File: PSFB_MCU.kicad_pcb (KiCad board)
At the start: 4 copper layers, 83 parts, among them Q1 WMM043N10HGD, Q2 WMM043N10HGD, Q3 WMM043N10HGD, Q4 WMM043N10HGD, U3 AMS1117-3.3, U4 LM5176PWP, U5 AMS1117-5.0

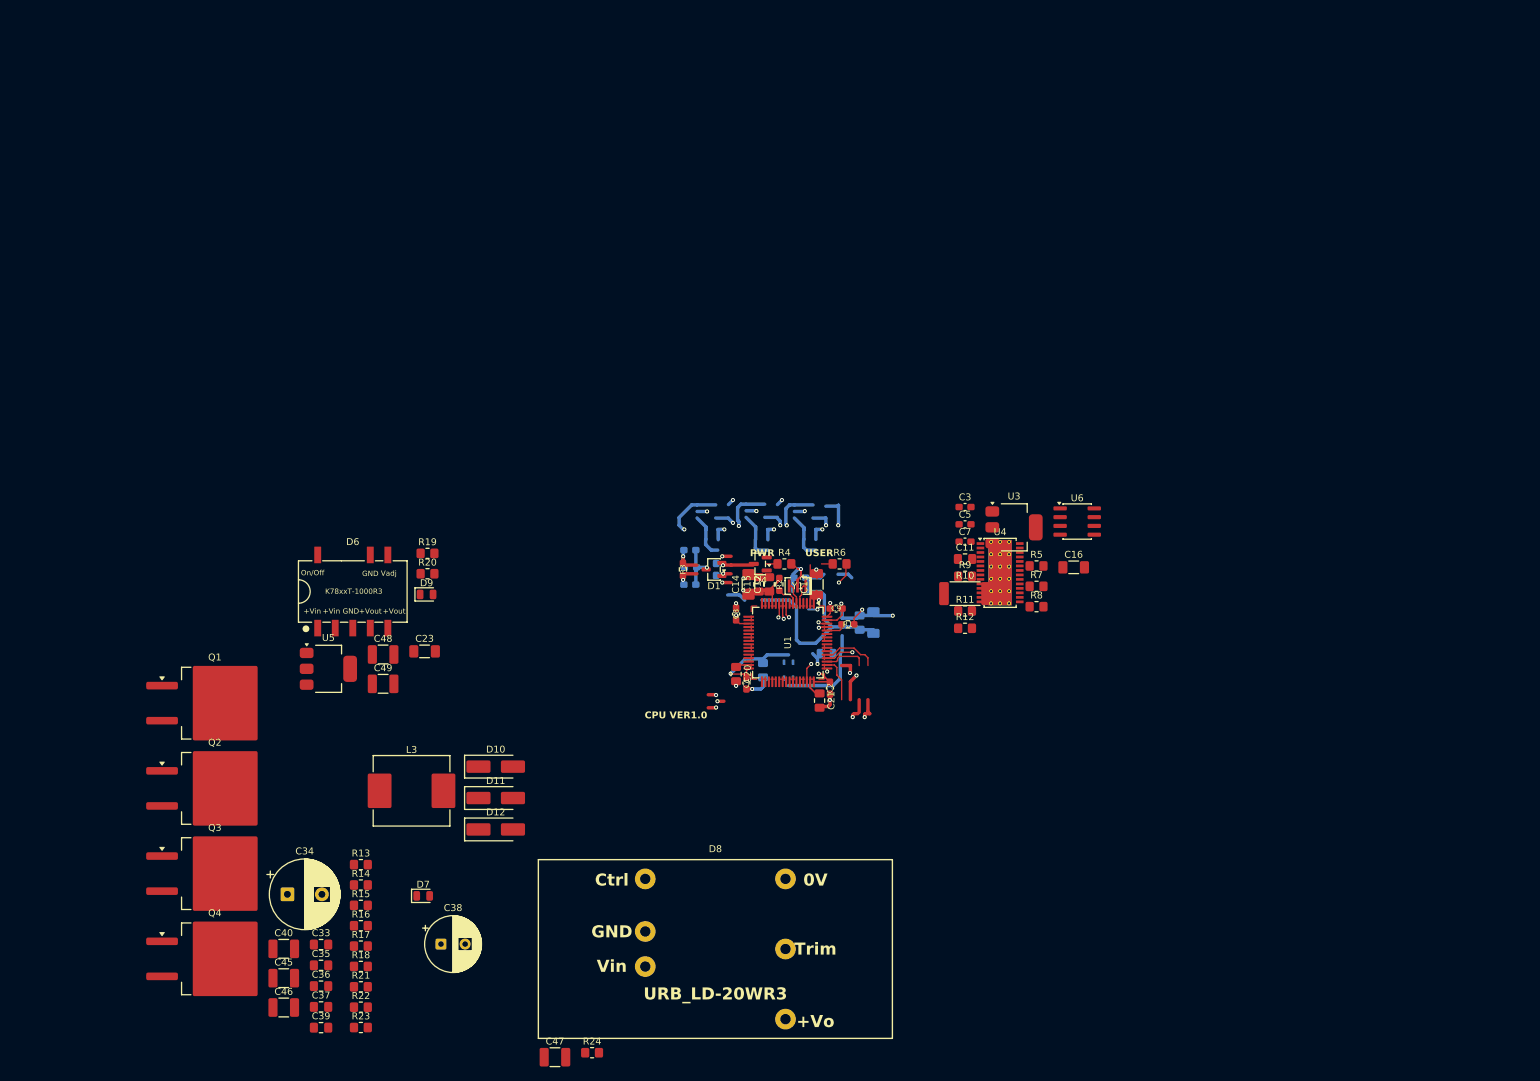
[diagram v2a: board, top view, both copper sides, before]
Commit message: VER1.0: добавил 4 канала управления драйверами
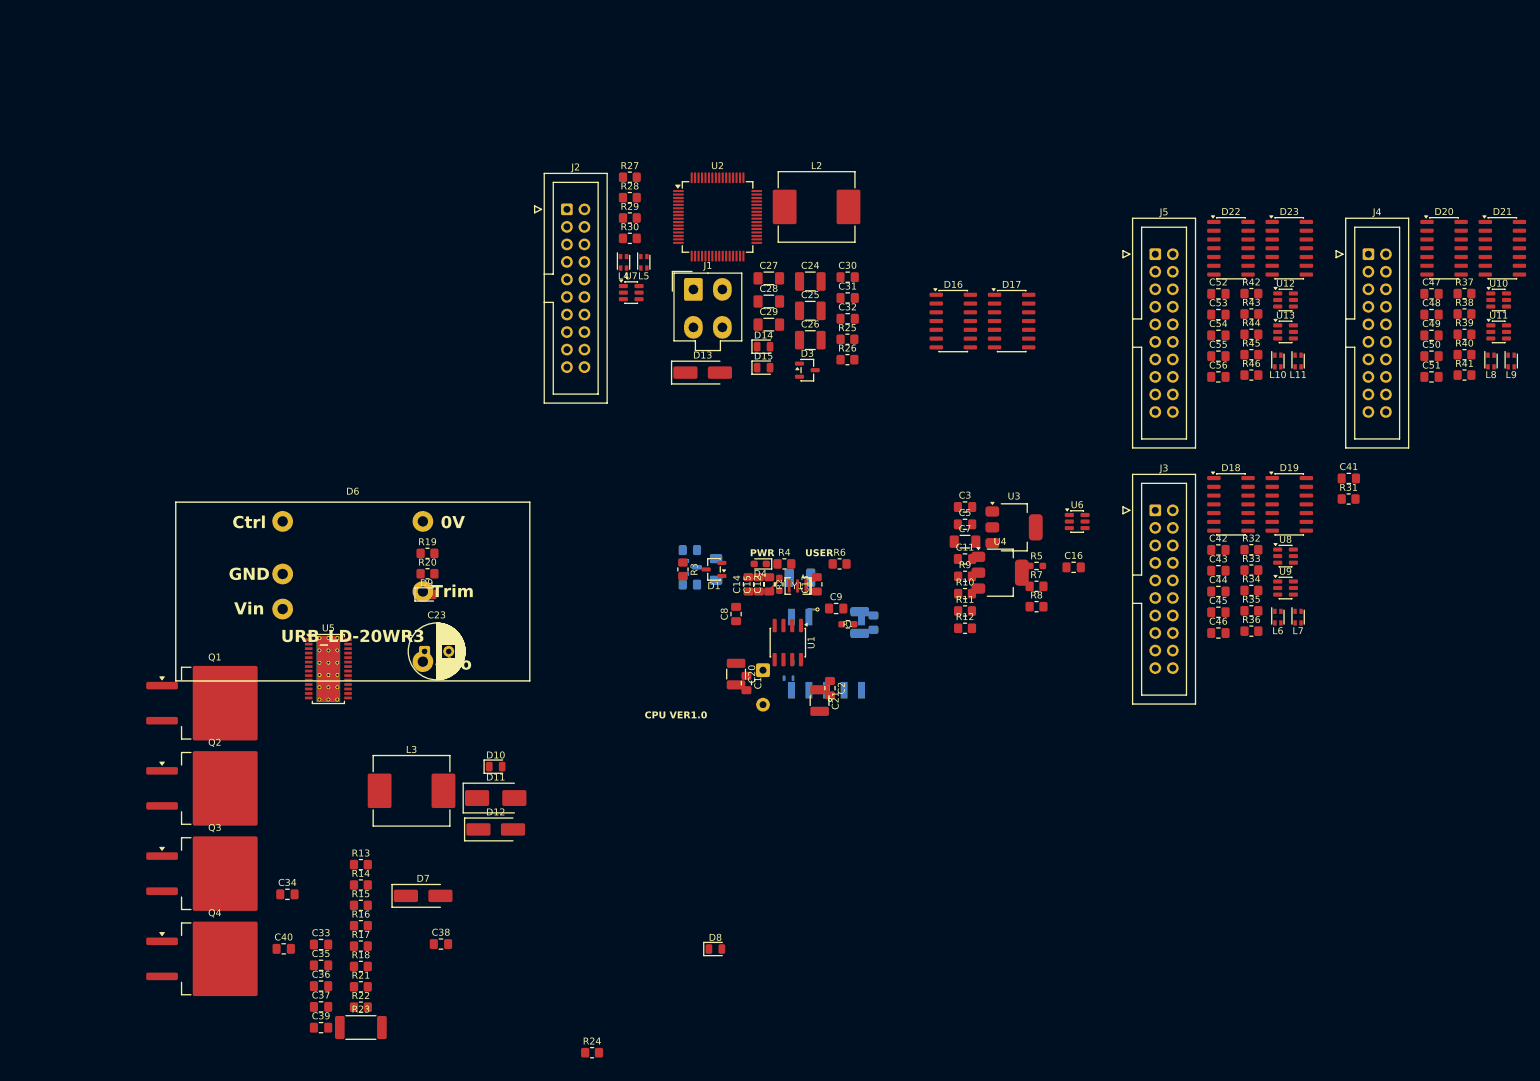
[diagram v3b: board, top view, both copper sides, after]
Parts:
- added C24: 10u, Capacitor_SMD:C_1210_3225Metric_Pad1.33x2.70mm_HandSolder, F.Cu at (151.3, 51.6)
- added C25: 10u, Capacitor_SMD:C_1210_3225Metric_Pad1.33x2.70mm_HandSolder, F.Cu at (151.3, 55.8)
- added C26: 10u, Capacitor_SMD:C_1210_3225Metric_Pad1.33x2.70mm_HandSolder, F.Cu at (151.3, 60.1)
- added C27: 10u, Capacitor_SMD:C_1206_3216Metric_Pad1.33x1.80mm_HandSolder, F.Cu at (145.2, 51.1)
- added C28: 10u, Capacitor_SMD:C_1206_3216Metric_Pad1.33x1.80mm_HandSolder, F.Cu at (145.2, 54.5)
- added C29: 10u, Capacitor_SMD:C_1206_3216Metric_Pad1.33x1.80mm_HandSolder, F.Cu at (145.2, 57.8)
- added C30: 33n, Capacitor_SMD:C_0805_2012Metric_Pad1.18x1.45mm_HandSolder, F.Cu at (156.7, 51.0)
- added C31: 100n, Capacitor_SMD:C_0805_2012Metric_Pad1.18x1.45mm_HandSolder, F.Cu at (156.7, 54.0)
- added C32: 560p, Capacitor_SMD:C_0805_2012Metric_Pad1.18x1.45mm_HandSolder, F.Cu at (156.7, 57.0)
- added C41: 10n, Capacitor_SMD:C_0805_2012Metric_Pad1.18x1.45mm_HandSolder, F.Cu at (229.3, 80.1)
- added C42: 100n, Capacitor_SMD:C_0805_2012Metric_Pad1.18x1.45mm_HandSolder, F.Cu at (210.4, 90.5)
- added C43: 4.7u, Capacitor_SMD:C_0805_2012Metric_Pad1.18x1.45mm_HandSolder, F.Cu at (210.4, 93.5)
- added C44: 100n, Capacitor_SMD:C_0805_2012Metric_Pad1.18x1.45mm_HandSolder, F.Cu at (210.4, 96.5)
- added C50: 4.7u, Capacitor_SMD:C_0805_2012Metric_Pad1.18x1.45mm_HandSolder, F.Cu at (241.3, 62.4)
- added C51: 10n, Capacitor_SMD:C_0805_2012Metric_Pad1.18x1.45mm_HandSolder, F.Cu at (241.3, 65.4)
- added C52: 100n, Capacitor_SMD:C_0805_2012Metric_Pad1.18x1.45mm_HandSolder, F.Cu at (210.4, 53.4)
- added C53: 4.7u, Capacitor_SMD:C_0805_2012Metric_Pad1.18x1.45mm_HandSolder, F.Cu at (210.4, 56.4)
- added C54: 100n, Capacitor_SMD:C_0805_2012Metric_Pad1.18x1.45mm_HandSolder, F.Cu at (210.4, 59.4)
- added C55: 4.7u, Capacitor_SMD:C_0805_2012Metric_Pad1.18x1.45mm_HandSolder, F.Cu at (210.4, 62.4)
- added C56: 10n, Capacitor_SMD:C_0805_2012Metric_Pad1.18x1.45mm_HandSolder, F.Cu at (210.4, 65.4)
- added D13: D_Schottky_Small, Diode_SMD:D_SMA_Handsoldering, F.Cu at (135.7, 64.8)
- added D14: ~, LED_SMD:LED_0805_2012Metric, F.Cu at (144.5, 61.0)
- added D15: ~, LED_SMD:LED_0805_2012Metric, F.Cu at (144.5, 64.1)
- added D16: DS90LV019, Package_SO:SO-14_3.9x8.65mm_P1.27mm, F.Cu at (172.0, 57.3)
- added D17: DS90LV019, Package_SO:SO-14_3.9x8.65mm_P1.27mm, F.Cu at (180.4, 57.3)
- added D18: DS90LV019, Package_SO:SO-14_3.9x8.65mm_P1.27mm, F.Cu at (212.2, 83.9)
- added D19: DS90LV019, Package_SO:SO-14_3.9x8.65mm_P1.27mm, F.Cu at (220.7, 83.9)
- added D20: DS90LV019, Package_SO:SO-14_3.9x8.65mm_P1.27mm, F.Cu at (243.1, 46.8)
- added D21: DS90LV019, Package_SO:SO-14_3.9x8.65mm_P1.27mm, F.Cu at (251.5, 46.8)
- added D22: DS90LV019, Package_SO:SO-14_3.9x8.65mm_P1.27mm, F.Cu at (212.2, 46.8)
- added D23: DS90LV019, Package_SO:SO-14_3.9x8.65mm_P1.27mm, F.Cu at (220.7, 46.8)
- added D3: ~, Package_TO_SOT_SMD:SOT-23-3, F.Cu at (150.8, 64.4)
- added J1: Power_IN, Connector_Molex:Molex_Mini-Fit_Jr_5566-04A_2x02_P4.20mm_Vertical, F.Cu at (134.3, 52.7)
- added J2: PSFB_Control_1, Connector_IDC:IDC-Header_2x10_P2.54mm_Vertical, F.Cu at (116.0, 41.1)
- added J3: PSFB_Control_1, Connector_IDC:IDC-Header_2x10_P2.54mm_Vertical, F.Cu at (201.2, 84.7)
- added J4: PSFB_Control_1, Connector_IDC:IDC-Header_2x10_P2.54mm_Vertical, F.Cu at (232.1, 47.6)
- added J5: PSFB_Control_1, Connector_IDC:IDC-Header_2x10_P2.54mm_Vertical, F.Cu at (201.2, 47.6)
- added L10: DLW21SN900SQ2L, Inductor_SMD:L_CommonModeChoke_Coilcraft_0805USB, F.Cu at (219.0, 63.1)
- added L11: DLW21SN900SQ2L, Inductor_SMD:L_CommonModeChoke_Coilcraft_0805USB, F.Cu at (221.9, 63.1)
- added L2: 10u, Inductor_SMD:L_Panasonic_PCC-M1040ML, F.Cu at (152.2, 40.8)
- added L4: DLW21SN900SQ2L, Inductor_SMD:L_CommonModeChoke_Coilcraft_0805USB, F.Cu at (124.2, 48.8)
- added L5: DLW21SN900SQ2L, Inductor_SMD:L_CommonModeChoke_Coilcraft_0805USB, F.Cu at (127.1, 48.8)
- added L6: DLW21SN900SQ2L, Inductor_SMD:L_CommonModeChoke_Coilcraft_0805USB, F.Cu at (219.0, 100.2)
- added L7: DLW21SN900SQ2L, Inductor_SMD:L_CommonModeChoke_Coilcraft_0805USB, F.Cu at (221.9, 100.2)
- added L8: DLW21SN900SQ2L, Inductor_SMD:L_CommonModeChoke_Coilcraft_0805USB, F.Cu at (249.9, 63.1)
- added L9: DLW21SN900SQ2L, Inductor_SMD:L_CommonModeChoke_Coilcraft_0805USB, F.Cu at (252.8, 63.1)
- added R25: 3k, Resistor_SMD:R_0805_2012Metric_Pad1.20x1.40mm_HandSolder, F.Cu at (156.6, 60.0)
- added R26: 3k, Resistor_SMD:R_0805_2012Metric_Pad1.20x1.40mm_HandSolder, F.Cu at (156.6, 62.9)
- added R27: 0, Resistor_SMD:R_0805_2012Metric_Pad1.20x1.40mm_HandSolder, F.Cu at (125.1, 36.5)
- added R28: 0, Resistor_SMD:R_0805_2012Metric_Pad1.20x1.40mm_HandSolder, F.Cu at (125.1, 39.4)
- added R29: 470, Resistor_SMD:R_0805_2012Metric_Pad1.20x1.40mm_HandSolder, F.Cu at (125.1, 42.4)
- added R30: 0, Resistor_SMD:R_0805_2012Metric_Pad1.20x1.40mm_HandSolder, F.Cu at (125.1, 45.3)
- added R31: 0, Resistor_SMD:R_0805_2012Metric_Pad1.20x1.40mm_HandSolder, F.Cu at (229.3, 83.1)
- added R32: 0, Resistor_SMD:R_0805_2012Metric_Pad1.20x1.40mm_HandSolder, F.Cu at (215.2, 90.4)
- added R33: 0, Resistor_SMD:R_0805_2012Metric_Pad1.20x1.40mm_HandSolder, F.Cu at (215.2, 93.4)
- added R34: 470, Resistor_SMD:R_0805_2012Metric_Pad1.20x1.40mm_HandSolder, F.Cu at (215.2, 96.3)
- added R35: 0, Resistor_SMD:R_0805_2012Metric_Pad1.20x1.40mm_HandSolder, F.Cu at (215.2, 99.3)
- added R36: 0, Resistor_SMD:R_0805_2012Metric_Pad1.20x1.40mm_HandSolder, F.Cu at (215.2, 102.2)
- added R37: 0, Resistor_SMD:R_0805_2012Metric_Pad1.20x1.40mm_HandSolder, F.Cu at (246.0, 53.3)
- added R38: 0, Resistor_SMD:R_0805_2012Metric_Pad1.20x1.40mm_HandSolder, F.Cu at (246.0, 56.3)
- added R39: 470, Resistor_SMD:R_0805_2012Metric_Pad1.20x1.40mm_HandSolder, F.Cu at (246.0, 59.2)
- added R40: 0, Resistor_SMD:R_0805_2012Metric_Pad1.20x1.40mm_HandSolder, F.Cu at (246.0, 62.2)
- added R41: 0, Resistor_SMD:R_0805_2012Metric_Pad1.20x1.40mm_HandSolder, F.Cu at (246.0, 65.1)
- added R42: 0, Resistor_SMD:R_0805_2012Metric_Pad1.20x1.40mm_HandSolder, F.Cu at (215.2, 53.3)
- added R43: 0, Resistor_SMD:R_0805_2012Metric_Pad1.20x1.40mm_HandSolder, F.Cu at (215.2, 56.3)
- added R44: 470, Resistor_SMD:R_0805_2012Metric_Pad1.20x1.40mm_HandSolder, F.Cu at (215.2, 59.2)
- added R45: 0, Resistor_SMD:R_0805_2012Metric_Pad1.20x1.40mm_HandSolder, F.Cu at (215.2, 62.2)
- added R46: 0, Resistor_SMD:R_0805_2012Metric_Pad1.20x1.40mm_HandSolder, F.Cu at (215.2, 65.1)
- added U10: USBLC6-2SC6, Package_TO_SOT_SMD:SOT-23-6, F.Cu at (251.0, 54.3)
- added U11: USBLC6-2SC6, Package_TO_SOT_SMD:SOT-23-6, F.Cu at (251.0, 58.9)
- added U12: USBLC6-2SC6, Package_TO_SOT_SMD:SOT-23-6, F.Cu at (220.1, 54.3)
- added U13: USBLC6-2SC6, Package_TO_SOT_SMD:SOT-23-6, F.Cu at (220.1, 58.9)
- added U2: ~, Package_QFP:LQFP-64_10x10mm_P0.5mm, F.Cu at (137.8, 42.2)
- added U7: USBLC6-2SC6, Package_TO_SOT_SMD:SOT-23-6, F.Cu at (125.3, 53.2)
- added U8: USBLC6-2SC6, Package_TO_SOT_SMD:SOT-23-6, F.Cu at (220.1, 91.4)
- added U9: USBLC6-2SC6, Package_TO_SOT_SMD:SOT-23-6, F.Cu at (220.1, 96.0)
- C1: value 100n -> 1u; footprint Capacitor_SMD:C_0603_1608Metric_Pad1.08x0.95mm_HandSolder -> Capacitor_SMD:C_0805_2012Metric_Pad1.18x1.45mm_HandSolder
- C10, C9: value 2.2u -> 100n; footprint Capacitor_SMD:C_0603_1608Metric_Pad1.08x0.95mm_HandSolder -> Capacitor_SMD:C_0805_2012Metric_Pad1.18x1.45mm_HandSolder
- C11: value 1u -> 4.7u
- C12: value 220p -> 1u
- C13: value 10u -> 2.2u; footprint Capacitor_SMD:C_1206_3216Metric_Pad1.33x1.80mm_HandSolder -> Capacitor_SMD:C_0805_2012Metric_Pad1.18x1.45mm_HandSolder
- C14: value 0.1u -> 2.2u; footprint Capacitor_SMD:C_1206_3216Metric_Pad1.33x1.80mm_HandSolder -> Capacitor_SMD:C_0805_2012Metric_Pad1.18x1.45mm_HandSolder
- C15: value 10n -> 100n
- C16: value 10u -> 1u; footprint Capacitor_SMD:C_1206_3216Metric_Pad1.33x1.80mm_HandSolder -> Capacitor_SMD:C_0805_2012Metric_Pad1.18x1.45mm_HandSolder
- C17: value 10u -> 100n; footprint Capacitor_SMD:C_1206_3216Metric_Pad1.33x1.80mm_HandSolder -> Capacitor_SMD:C_0805_2012Metric_Pad1.18x1.45mm_HandSolder
- C18: value 100n -> 2.2u; footprint Capacitor_SMD:C_0805_2012Metric_Pad1.18x1.45mm_HandSolder -> Capacitor_SMD:C_1210_3225Metric_Pad1.33x2.70mm_HandSolder
- C19: value 47p -> 100u; footprint Capacitor_SMD:C_0805_2012Metric_Pad1.18x1.45mm_HandSolder -> Capacitor_THT:CP_Radial_D10.0mm_P5.00mm
- C2, C3, C4, C5: footprint Capacitor_SMD:C_0603_1608Metric_Pad1.08x0.95mm_HandSolder -> Capacitor_SMD:C_0805_2012Metric_Pad1.18x1.45mm_HandSolder
- C20: value 1n -> 4.7u; footprint Capacitor_SMD:C_0805_2012Metric_Pad1.18x1.45mm_HandSolder -> Capacitor_SMD:C_1210_3225Metric_Pad1.33x2.70mm_HandSolder
- C21: value 33n -> 10u; footprint Capacitor_SMD:C_0805_2012Metric_Pad1.18x1.45mm_HandSolder -> Capacitor_SMD:C_1210_3225Metric_Pad1.33x2.70mm_HandSolder
- C22: value 1u -> 10u; footprint Capacitor_SMD:C_0603_1608Metric_Pad1.08x0.95mm_HandSolder -> Capacitor_SMD:C_1210_3225Metric_Pad1.33x2.70mm_HandSolder
- C23: value 10u -> 220u; footprint Capacitor_SMD:C_1206_3216Metric_Pad1.33x1.80mm_HandSolder -> Capacitor_THT:CP_Radial_D8.0mm_P3.50mm
- C33: value 560p -> 100n
- C34: value 100u -> 220p; footprint Capacitor_THT:CP_Radial_D10.0mm_P5.00mm -> Capacitor_SMD:C_0805_2012Metric_Pad1.18x1.45mm_HandSolder
- C36: value 100n -> 47p
- C38: value 220u -> 4.7u; footprint Capacitor_THT:CP_Radial_D8.0mm_P3.50mm -> Capacitor_SMD:C_0805_2012Metric_Pad1.18x1.45mm_HandSolder
- C40: footprint Capacitor_SMD:C_1210_3225Metric_Pad1.33x2.70mm_HandSolder -> Capacitor_SMD:C_0805_2012Metric_Pad1.18x1.45mm_HandSolder
- C45, C48: value 10u -> 4.7u; footprint Capacitor_SMD:C_1210_3225Metric_Pad1.33x2.70mm_HandSolder -> Capacitor_SMD:C_0805_2012Metric_Pad1.18x1.45mm_HandSolder
- C46: value 10u -> 10n; footprint Capacitor_SMD:C_1210_3225Metric_Pad1.33x2.70mm_HandSolder -> Capacitor_SMD:C_0805_2012Metric_Pad1.18x1.45mm_HandSolder
- C47, C49: value 10u -> 100n; footprint Capacitor_SMD:C_1210_3225Metric_Pad1.33x2.70mm_HandSolder -> Capacitor_SMD:C_0805_2012Metric_Pad1.18x1.45mm_HandSolder
- C6: value 100n -> 10u; footprint Capacitor_SMD:C_0603_1608Metric_Pad1.08x0.95mm_HandSolder -> Capacitor_SMD:C_1206_3216Metric_Pad1.33x1.80mm_HandSolder
- C7: value 4.7u -> 0.1u; footprint Capacitor_SMD:C_0603_1608Metric_Pad1.08x0.95mm_HandSolder -> Capacitor_SMD:C_1206_3216Metric_Pad1.33x1.80mm_HandSolder
- C8: value 1u -> 10n; footprint Capacitor_SMD:C_0603_1608Metric_Pad1.08x0.95mm_HandSolder -> Capacitor_SMD:C_0805_2012Metric_Pad1.18x1.45mm_HandSolder
- D1: value ~ -> TD301MCANFD
- D10: value D_Schottky_Small -> ~; footprint Diode_SMD:D_SMA_Handsoldering -> LED_SMD:LED_0805_2012Metric
- D11: value D_Schottky_Small -> D_TVS_Small; footprint Diode_SMD:D_SMA_Handsoldering -> Diode_SMD:D_SMB_Handsoldering
- D2: footprint LED_SMD:LED_0603_1608Metric_Pad1.05x0.95mm_HandSolder -> Package_TO_SOT_SMD:SOT-23
- D4: footprint Package_TO_SOT_SMD:SOT-23 -> LED_SMD:LED_0603_1608Metric_Pad1.05x0.95mm_HandSolder
- D5: value ~ -> K7809T; footprint LED_SMD:LED_0805_2012Metric -> MORNSUN:K78xxT-1000R3
- D6: value K7809T -> URB2415LD-20WR3; footprint MORNSUN:K78xxT-1000R3 -> MORNSUN:URB_LD-20WR3
- D7: value ~ -> D_Schottky_Small; footprint LED_SMD:LED_0805_2012Metric -> Diode_SMD:D_SMA_Handsoldering
- D8: value URB2415LD-20WR3 -> ~; footprint MORNSUN:URB_LD-20WR3 -> LED_SMD:LED_0805_2012Metric
- R10: value 10m -> 3k; footprint Resistor_SMD:R_2512_6332Metric_Pad1.40x3.35mm_HandSolder -> Resistor_SMD:R_0805_2012Metric_Pad1.20x1.40mm_HandSolder
- R11: value 143k -> 1k
- R12: value 10k -> 249k
- R14: value 249k -> 10k
- R15: value 10 -> 240k
- R16: value 2k -> 93.1k
- R17: value 10k -> 51k
- R18: value 0 -> 143k
- R19: value 1k -> 10k
- R20: value 3k -> 10k
- R21: value 10k -> 100
- R22: value 240k -> 0
- R23: value 51k -> 10m; footprint Resistor_SMD:R_0805_2012Metric_Pad1.20x1.40mm_HandSolder -> Resistor_SMD:R_2512_6332Metric_Pad1.40x3.35mm_HandSolder
- R24: value 0 -> 100
- R3: value 1k -> 59; footprint Resistor_SMD:R_0603_1608Metric_Pad0.98x0.95mm_HandSolder -> Resistor_SMD:R_0805_2012Metric_Pad1.20x1.40mm_HandSolder
- R4: value 93.1k -> 59
- R5: value 59 -> 1k; footprint Resistor_SMD:R_0805_2012Metric_Pad1.20x1.40mm_HandSolder -> Resistor_SMD:R_0603_1608Metric_Pad0.98x0.95mm_HandSolder
- R6: value 100 -> 2k
- R7: value 59 -> 10
- R9: value 100 -> 0
- U1: footprint Package_QFP:LQFP-64_10x10mm_P0.5mm -> Package_SO:SOIC-8_3.9x4.9mm_P1.27mm
- U3: value AMS1117-3.3 -> AMS1117-5.0
- U4: value LM5176PWP -> AMS1117-3.3; footprint Package_SO:HTSSOP-28-1EP_4.4x9.7mm_P0.65mm_EP3.4x9.5mm_ThermalVias -> Package_TO_SOT_SMD:SOT-223-3_TabPin2
- U5: value AMS1117-5.0 -> LM5176PWP; footprint Package_TO_SOT_SMD:SOT-223-3_TabPin2 -> Package_SO:HTSSOP-28-1EP_4.4x9.7mm_P0.65mm_EP3.4x9.5mm_ThermalVias
- U6: value ~ -> USBLC6-2SC6; footprint Package_SO:SOIC-8_3.9x4.9mm_P1.27mm -> Package_TO_SOT_SMD:SOT-23-6
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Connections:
- C10 pad 1: Net-(U1-VCAP_2) -> +3.3V
- C11 pad 1: VCC -> +3.3V
- C11 pad 2: GND_IN -> GND
- C12 pad 1: Net-(U4-SLOPE) -> +3.3V
- C12 pad 2: GND_IN -> GND
- C13 pad 1: +3.3V -> Net-(U2-VCAP_1)
- C14 pad 1: +3.3V -> Net-(U2-VCAP_2)
- C15 pad 1: Net-(C15-Pad1) -> Net-(U5-VIN)
- C15 pad 2: GND_CAN -> GND_IN
- C16 pad 1: GND -> VCC
- C16 pad 2: +5V -> GND_IN
- C17 pad 1: GND -> +24V
- C17 pad 2: +3.3V -> GND_IN
- C18 pad 1: Net-(U4-SS) -> GND_IN
- C18 pad 2: GND_IN -> VIN_filtered
- C19 pad 1: Net-(U4-CSG) -> VIN_filtered
- C19 pad 2: Net-(U4-CS) -> GND_IN
- C20 pad 1: Net-(U4-RT/SYNC) -> GND_IN
- C20 pad 2: unconnected-(C20-Pad2) -> VIN_filtered
- C21 pad 1: Net-(U4-COMP) -> GND_IN
- C21 pad 2: Net-(C21-Pad2) -> +24V
- C22 pad 1: +3.3V -> GND_IN
- C22 pad 2: GND -> +24V
- C23 pad 1: GND -> +24V
- C23 pad 2: +5V -> GND_IN
- C33 pad 1: Net-(U4-COMP) -> /SW1
- C33 pad 2: GND_IN -> Net-(D12-K)
- C34 pad 1: VIN -> Net-(U5-SLOPE)
- C35 pad 1: Net-(U4-VIN) -> /SW2
- C35 pad 2: GND_IN -> Net-(D13-K)
- C36 pad 1: /SW1 -> Net-(U5-CSG)
- C36 pad 2: Net-(D10-K) -> Net-(U5-CS)
- C37 pad 1: /SW2 -> +3.3V
- C37 pad 2: Net-(D11-K) -> GND
- C38 pad 1: +24V -> +3.3V
- C38 pad 2: GND_IN -> GND
- C39 pad 1: +24V -> +3.3V
- C39 pad 2: GND_IN -> GND
- C40 pad 1: GND_IN -> +3.3V
- C40 pad 2: VIN -> GND
- C45 pad 1: GND_IN -> +3.3V
- C45 pad 2: +24V -> GND
- C46 pad 1: GND_IN -> /FAULT2
- C46 pad 2: +24V -> GND
- C47 pad 1: GND_IN -> +3.3V
- C47 pad 2: +24V -> GND
- C48 pad 1: GND -> +3.3V
- C48 pad 2: +9V -> GND
- C49 pad 1: GND -> +3.3V
- C49 pad 2: +15V -> GND
- C8 pad 1: +3.3V -> Net-(C8-Pad1)
- C8 pad 2: GND -> GND_CAN
- C9 pad 1: Net-(U1-VCAP_1) -> +3.3V
- D1 pad 1: SWCLK -> CAN1_RXD_MCU
- D1 pad 2: SWDIO -> CAN1_TXD_MCU
- D10 pad 2: VCC -> +3.3V
- D11 pad 1: Net-(D11-K) -> GND_IN
- D11 pad 2: VCC -> VIN_filtered
- D12 pad 2: VIN -> VCC
- D2 pad 1: Net-(D2-K) -> CANH
- D2 pad 2: Net-(D2-A) -> CANL
- D4 pad 1: CANH -> Net-(D4-K)
- D4 pad 2: CANL -> Net-(D4-A)
- D5 pad 1: Net-(D5-K) -> +15V
- D5 pad 2: +3.3V -> +15V
- D6 pad 1: +15V -> unconnected-(D6-Ctrl-Pad1)
- D6 pad 2: +15V -> GND_IN
- D6 pad 3: GND -> +24V
- D6 pad 4: +9V -> +15V
- D6 pad 5: +9V -> Net-(D6-Trim)
- D6 pad 6: unconnected-(D6-Vadj-Pad6) -> GND1
- D7 pad 2: +5V -> VIN_filtered
- D8 pad 1: unconnected-(D8-Ctrl-Pad1) -> Net-(D8-K)
- D8 pad 2: GND_IN -> +5V
- L1 pad 1: Net-(D3-CANH) -> Net-(D1-CANH)
- L1 pad 3: Net-(D3-CANL) -> Net-(D1-CANL)
- Q1 pad 2: VIN -> VIN_filtered
- Q2 pad 1: /LDRV1 -> /HDRV2
- Q2 pad 2: /SW1 -> +24V
- Q2 pad 3: Net-(Q2-S) -> /SW2
- Q3 pad 1: /HDRV2 -> /LDRV1
- Q3 pad 2: +24V -> /SW1
- Q3 pad 3: /SW2 -> Net-(Q3-S)
- Q4 pad 3: Net-(Q2-S) -> Net-(Q3-S)
- R10 pad 1: GND_IN -> Net-(D9-K)
- R10 pad 2: Net-(Q2-S) -> GND
- R11 pad 1: GND_IN -> Net-(D10-K)
- R11 pad 2: Net-(U4-RT/SYNC) -> GND
- R12 pad 1: GND_IN -> Net-(U5-EN/UVLO)
- R12 pad 2: Net-(C21-Pad2) -> VIN_filtered
- R13 pad 1: Net-(U4-EN/UVLO) -> Net-(U5-EN/UVLO)
- R14 pad 1: Net-(U4-EN/UVLO) -> GND_IN
- R14 pad 2: VIN -> Net-(C30-Pad2)
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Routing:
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- removed copper zone on F.Cu, net GND

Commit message: VER1.0: добавил схему с измерением напряжения и заменил LVDS трансиверы
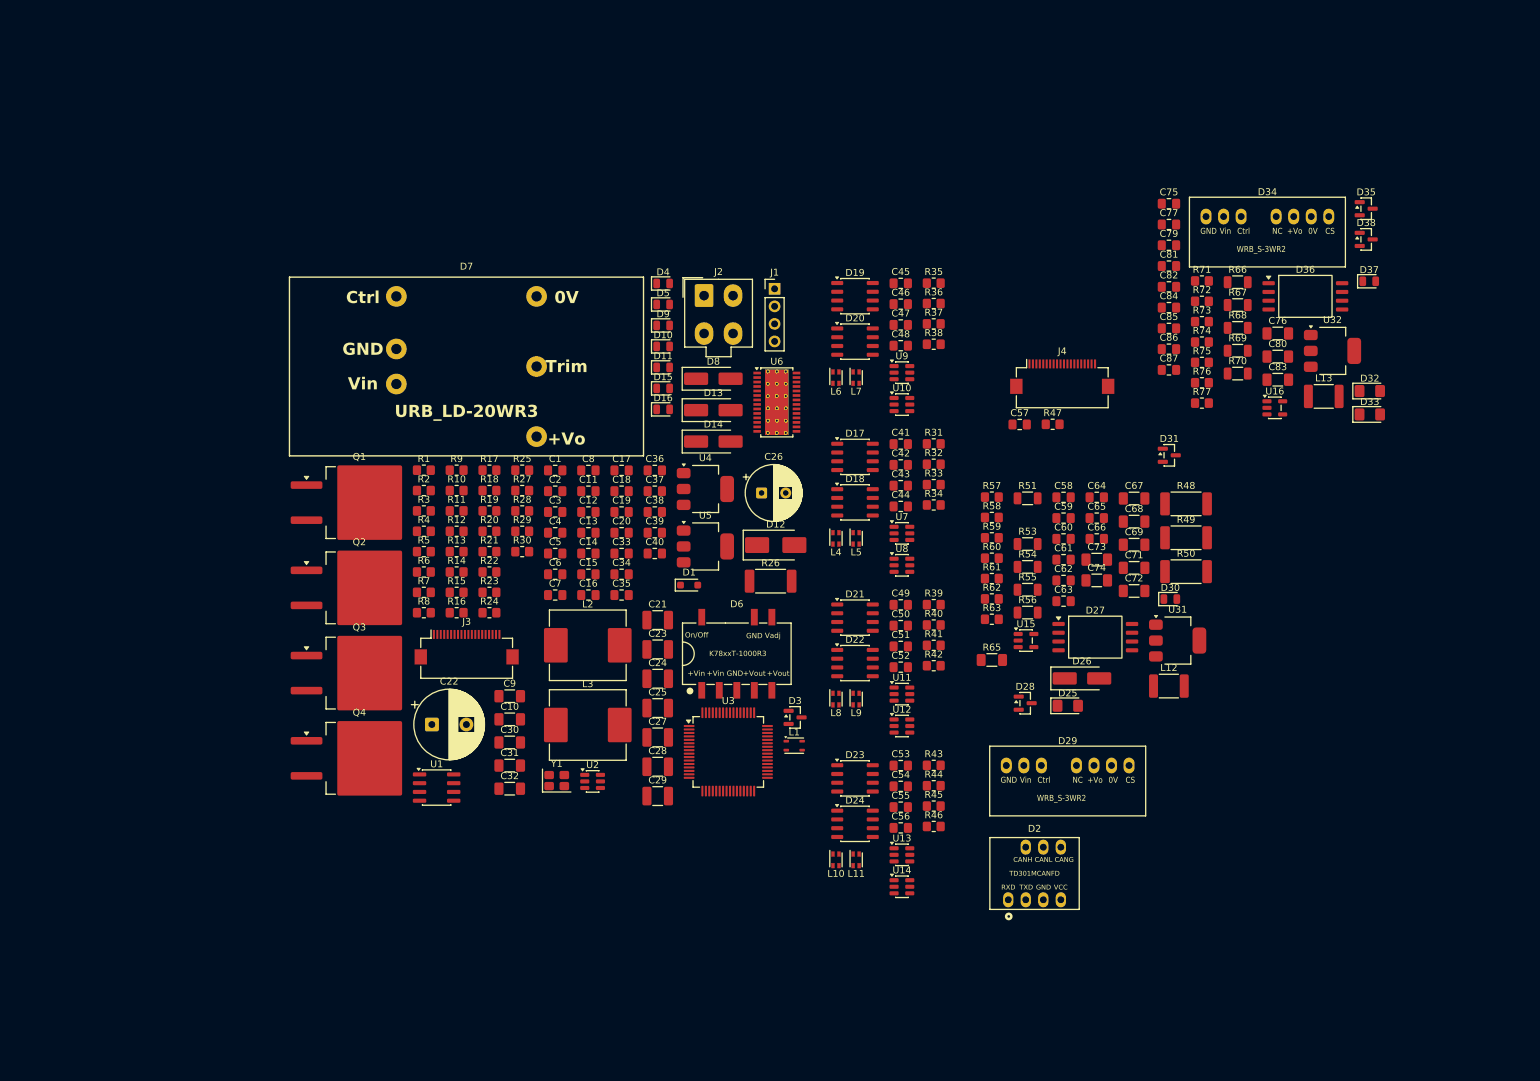
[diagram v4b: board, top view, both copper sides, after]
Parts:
- removed J5: PSFB_Control_1, Connector_IDC:IDC-Header_2x10_P2.54mm_Vertical
- added C57: 10n, Capacitor_SMD:C_0805_2012Metric_Pad1.18x1.45mm_HandSolder, F.Cu at (181.6, 72.3)
- added C58: 56p, Capacitor_SMD:C_0805_2012Metric_Pad1.18x1.45mm_HandSolder, F.Cu at (187.9, 82.8)
- added C59: 2.2u, Capacitor_SMD:C_0805_2012Metric_Pad1.18x1.45mm_HandSolder, F.Cu at (187.9, 85.9)
- added C60: 0.1u, Capacitor_SMD:C_0805_2012Metric_Pad1.18x1.45mm_HandSolder, F.Cu at (187.9, 88.9)
- added C61: 2.2u, Capacitor_SMD:C_0805_2012Metric_Pad1.18x1.45mm_HandSolder, F.Cu at (187.9, 91.9)
- added C62: 0.1u, Capacitor_SMD:C_0805_2012Metric_Pad1.18x1.45mm_HandSolder, F.Cu at (187.9, 94.9)
- added C63: 56p, Capacitor_SMD:C_0805_2012Metric_Pad1.18x1.45mm_HandSolder, F.Cu at (187.9, 97.9)
- added C64: 56p, Capacitor_SMD:C_0805_2012Metric_Pad1.18x1.45mm_HandSolder, F.Cu at (192.8, 82.8)
- added C65: 100n, Capacitor_SMD:C_0805_2012Metric_Pad1.18x1.45mm_HandSolder, F.Cu at (192.8, 85.9)
- added C66: 1n, Capacitor_SMD:C_0805_2012Metric_Pad1.18x1.45mm_HandSolder, F.Cu at (192.8, 88.9)
- added C67: 10u, Capacitor_SMD:C_1206_3216Metric_Pad1.33x1.80mm_HandSolder, F.Cu at (198.2, 83.0)
- added C68: 1u, Capacitor_SMD:C_1206_3216Metric_Pad1.33x1.80mm_HandSolder, F.Cu at (198.2, 86.4)
- added C69: 10u, Capacitor_SMD:C_1206_3216Metric_Pad1.33x1.80mm_HandSolder, F.Cu at (198.2, 89.7)
- added C71: 10u, Capacitor_SMD:C_1206_3216Metric_Pad1.33x1.80mm_HandSolder, F.Cu at (198.2, 93.1)
- added C72: 10u, Capacitor_SMD:C_1206_3216Metric_Pad1.33x1.80mm_HandSolder, F.Cu at (198.2, 96.4)
- added C73: 10u, Capacitor_SMD:C_1206_3216Metric_Pad1.33x1.80mm_HandSolder, F.Cu at (192.8, 91.9)
- added C74: 1u, Capacitor_SMD:C_1206_3216Metric_Pad1.33x1.80mm_HandSolder, F.Cu at (192.8, 94.9)
- added C75: 56p, Capacitor_SMD:C_0805_2012Metric_Pad1.18x1.45mm_HandSolder, F.Cu at (203.2, 40.3)
- added C76: 10u, Capacitor_SMD:C_1206_3216Metric_Pad1.33x1.80mm_HandSolder, F.Cu at (219.0, 59.1)
- added C77: 2.2u, Capacitor_SMD:C_0805_2012Metric_Pad1.18x1.45mm_HandSolder, F.Cu at (203.2, 43.3)
- added C79: 0.1u, Capacitor_SMD:C_0805_2012Metric_Pad1.18x1.45mm_HandSolder, F.Cu at (203.2, 46.3)
- added C80: 10u, Capacitor_SMD:C_1206_3216Metric_Pad1.33x1.80mm_HandSolder, F.Cu at (219.0, 62.5)
- added C81: 2.2u, Capacitor_SMD:C_0805_2012Metric_Pad1.18x1.45mm_HandSolder, F.Cu at (203.2, 49.3)
- added C82: 0.1u, Capacitor_SMD:C_0805_2012Metric_Pad1.18x1.45mm_HandSolder, F.Cu at (203.2, 52.4)
- added C83: 10u, Capacitor_SMD:C_1206_3216Metric_Pad1.33x1.80mm_HandSolder, F.Cu at (219.0, 65.8)
- added C84: 56p, Capacitor_SMD:C_0805_2012Metric_Pad1.18x1.45mm_HandSolder, F.Cu at (203.2, 55.4)
- added C85: 56p, Capacitor_SMD:C_0805_2012Metric_Pad1.18x1.45mm_HandSolder, F.Cu at (203.2, 58.4)
- added C86: 100n, Capacitor_SMD:C_0805_2012Metric_Pad1.18x1.45mm_HandSolder, F.Cu at (203.2, 61.4)
- added C87: 1n, Capacitor_SMD:C_0805_2012Metric_Pad1.18x1.45mm_HandSolder, F.Cu at (203.2, 64.4)
- added D24: ~, Package_SO:SO-8_3.9x4.9mm_P1.27mm, F.Cu at (157.7, 130.2)
- added D25: ~, LED_SMD:LED_1206_3216Metric_Pad1.42x1.75mm_HandSolder, F.Cu at (188.6, 113.1)
- added D26: ~, Diode_SMD:D_SMA_Handsoldering, F.Cu at (190.6, 109.1)
- added D27: ~, Package_SO:SOIC-8_7.5x5.85mm_P1.27mm, F.Cu at (192.6, 103.1)
- added D28: ~, Package_TO_SOT_SMD:SOT-23, F.Cu at (182.4, 112.7)
- added D29: ~, MORNSUN:WRB_S-3WR2, F.Cu at (188.5, 121.7)
- added D30: ~, LED_SMD:LED_0805_2012Metric, F.Cu at (203.4, 97.6)
- added D31: ~, Package_TO_SOT_SMD:SOT-23, F.Cu at (203.3, 76.8)
- added D32: ~, LED_SMD:LED_1206_3216Metric_Pad1.42x1.75mm_HandSolder, F.Cu at (232.3, 67.5)
- added D33: ~, LED_SMD:LED_1206_3216Metric_Pad1.42x1.75mm_HandSolder, F.Cu at (232.3, 70.8)
- added D34: ~, MORNSUN:WRB_S-3WR2, F.Cu at (217.5, 42.2)
- added D35: ~, Package_TO_SOT_SMD:SOT-23, F.Cu at (231.8, 41.0)
- added D36: ~, Package_SO:SOIC-8_7.5x5.85mm_P1.27mm, F.Cu at (223.0, 53.7)
- added D37: ~, LED_SMD:LED_0805_2012Metric, F.Cu at (232.2, 51.5)
- added D38: ~, Package_TO_SOT_SMD:SOT-23, F.Cu at (231.8, 45.5)
- added L12: 4.7u, Inductor_SMD:L_1812_4532Metric_Pad1.30x3.40mm_HandSolder, F.Cu at (203.2, 110.2)
- added L13: 4.7u, Inductor_SMD:L_1812_4532Metric_Pad1.30x3.40mm_HandSolder, F.Cu at (225.7, 68.2)
- added R47: 470, Resistor_SMD:R_0805_2012Metric_Pad1.20x1.40mm_HandSolder, F.Cu at (186.4, 72.3)
- added R48: 150k, Resistor_SMD:R_2512_6332Metric_Pad1.40x3.35mm_HandSolder, F.Cu at (205.7, 83.8)
- added R49: 150k, Resistor_SMD:R_2512_6332Metric_Pad1.40x3.35mm_HandSolder, F.Cu at (205.7, 88.7)
- added R50: 150k, Resistor_SMD:R_2512_6332Metric_Pad1.40x3.35mm_HandSolder, F.Cu at (205.7, 93.6)
- added R51: 2M, Resistor_SMD:R_1206_3216Metric, F.Cu at (182.7, 83.0)
- added R53: 2M, Resistor_SMD:R_1206_3216Metric, F.Cu at (182.7, 89.6)
- added R54: 2M, Resistor_SMD:R_1206_3216Metric, F.Cu at (182.7, 92.9)
- added R55: 2M, Resistor_SMD:R_1206_3216Metric, F.Cu at (182.7, 96.2)
- added R56: 11.3k, Resistor_SMD:R_1206_3216Metric, F.Cu at (182.7, 99.5)
- added R57: 120, Resistor_SMD:R_0805_2012Metric_Pad1.20x1.40mm_HandSolder, F.Cu at (177.6, 82.8)
- added R58: 1k, Resistor_SMD:R_0805_2012Metric_Pad1.20x1.40mm_HandSolder, F.Cu at (177.6, 85.8)
- added R59: 1k, Resistor_SMD:R_0805_2012Metric_Pad1.20x1.40mm_HandSolder, F.Cu at (177.6, 88.7)
- added R60: 1k, Resistor_SMD:R_0805_2012Metric_Pad1.20x1.40mm_HandSolder, F.Cu at (177.6, 91.7)
- added R61: 1k, Resistor_SMD:R_0805_2012Metric_Pad1.20x1.40mm_HandSolder, F.Cu at (177.6, 94.6)
- added R62: 510, Resistor_SMD:R_0805_2012Metric_Pad1.20x1.40mm_HandSolder, F.Cu at (177.6, 97.6)
- added R63: 750, Resistor_SMD:R_0805_2012Metric_Pad1.20x1.40mm_HandSolder, F.Cu at (177.6, 100.5)
- added R65: 10k, Resistor_SMD:R_1206_3216Metric_Pad1.30x1.75mm_HandSolder, F.Cu at (177.6, 106.4)
- added R66: 110k, Resistor_SMD:R_1206_3216Metric, F.Cu at (213.2, 51.7)
- added R67: 110k, Resistor_SMD:R_1206_3216Metric, F.Cu at (213.2, 55.0)
- added R68: 110k, Resistor_SMD:R_1206_3216Metric, F.Cu at (213.2, 58.3)
- added R69: 110k, Resistor_SMD:R_1206_3216Metric, F.Cu at (213.2, 61.6)
- added R70: 11.3k, Resistor_SMD:R_1206_3216Metric, F.Cu at (213.2, 64.9)
- added R71: 120, Resistor_SMD:R_0805_2012Metric_Pad1.20x1.40mm_HandSolder, F.Cu at (208.0, 51.5)
- added R72: 1k, Resistor_SMD:R_0805_2012Metric_Pad1.20x1.40mm_HandSolder, F.Cu at (208.0, 54.5)
- added R73: 1k, Resistor_SMD:R_0805_2012Metric_Pad1.20x1.40mm_HandSolder, F.Cu at (208.0, 57.4)
- added R74: 750, Resistor_SMD:R_0805_2012Metric_Pad1.20x1.40mm_HandSolder, F.Cu at (208.0, 60.4)
- added R75: 1k, Resistor_SMD:R_0805_2012Metric_Pad1.20x1.40mm_HandSolder, F.Cu at (208.0, 63.3)
- added R76: 1k, Resistor_SMD:R_0805_2012Metric_Pad1.20x1.40mm_HandSolder, F.Cu at (208.0, 66.2)
- added R77: 510, Resistor_SMD:R_0805_2012Metric_Pad1.20x1.40mm_HandSolder, F.Cu at (208.0, 69.2)
- added U14: USBLC6-2SC6, Package_TO_SOT_SMD:SOT-23-6, F.Cu at (164.5, 139.3)
- added U15: ~, Package_TO_SOT_SMD:SOT-23-5, F.Cu at (182.5, 103.6)
- added U16: ~, Package_TO_SOT_SMD:SOT-23-5, F.Cu at (218.6, 69.9)
- added U31: ~, Package_TO_SOT_SMD:SOT-223-3_TabPin2, F.Cu at (204.5, 103.6)
- added U32: ~, Package_TO_SOT_SMD:SOT-223-3_TabPin2, F.Cu at (226.9, 61.6)
- C10: value 100n -> 0.1u; footprint Capacitor_SMD:C_0805_2012Metric_Pad1.18x1.45mm_HandSolder -> Capacitor_SMD:C_1206_3216Metric_Pad1.33x1.80mm_HandSolder; moved to F.Cu
- C11, C40: value 4.7u -> 10n
- C12: value 1u -> 2.2u
- C14: value 2.2u -> 100n
- C16: value 1u -> 4.7u
- C17: value 100n -> 1u; moved to F.Cu
- C18: value 2.2u -> 100n; footprint Capacitor_SMD:C_1210_3225Metric_Pad1.33x2.70mm_HandSolder -> Capacitor_SMD:C_0805_2012Metric_Pad1.18x1.45mm_HandSolder; moved to F.Cu
- C19: value 100u -> 1u; footprint Capacitor_THT:CP_Radial_D10.0mm_P5.00mm -> Capacitor_SMD:C_0805_2012Metric_Pad1.18x1.45mm_HandSolder; moved to F.Cu
- C20: value 4.7u -> 100n; footprint Capacitor_SMD:C_1210_3225Metric_Pad1.33x2.70mm_HandSolder -> Capacitor_SMD:C_0805_2012Metric_Pad1.18x1.45mm_HandSolder
- C21: value 10u -> 2.2u
- C22: value 10u -> 100u; footprint Capacitor_SMD:C_1210_3225Metric_Pad1.33x2.70mm_HandSolder -> Capacitor_THT:CP_Radial_D10.0mm_P5.00mm; moved to F.Cu
- C23: value 220u -> 4.7u; footprint Capacitor_THT:CP_Radial_D8.0mm_P3.50mm -> Capacitor_SMD:C_1210_3225Metric_Pad1.33x2.70mm_HandSolder
- C26: value 10u -> 220u; footprint Capacitor_SMD:C_1210_3225Metric_Pad1.33x2.70mm_HandSolder -> Capacitor_THT:CP_Radial_D8.0mm_P3.50mm
- C27, C28, C29: footprint Capacitor_SMD:C_1206_3216Metric_Pad1.33x1.80mm_HandSolder -> Capacitor_SMD:C_1210_3225Metric_Pad1.33x2.70mm_HandSolder
- C3: value 100n -> 12p
- C30: value 33n -> 10u; footprint Capacitor_SMD:C_0805_2012Metric_Pad1.18x1.45mm_HandSolder -> Capacitor_SMD:C_1206_3216Metric_Pad1.33x1.80mm_HandSolder
- C31, C9: value 100n -> 10u; footprint Capacitor_SMD:C_0805_2012Metric_Pad1.18x1.45mm_HandSolder -> Capacitor_SMD:C_1206_3216Metric_Pad1.33x1.80mm_HandSolder
- C32: value 560p -> 10u; footprint Capacitor_SMD:C_0805_2012Metric_Pad1.18x1.45mm_HandSolder -> Capacitor_SMD:C_1206_3216Metric_Pad1.33x1.80mm_HandSolder
- C33: value 100n -> 33n
- C34: value 220p -> 100n
- C35: value 100n -> 560p
- C36: value 47p -> 100n
- C37: value 100n -> 220p
- C38, C43, C45, C50, C53: value 4.7u -> 100n
- C39: value 100n -> 47p
- C4: value 100n -> 12p; moved to F.Cu
- C41, C46, C8: value 10n -> 100n
- C42, C44, C47, C52: value 100n -> 4.7u
- C51, C56: value 10n -> 4.7u
- C6: value 10u -> 100n; footprint Capacitor_SMD:C_1206_3216Metric_Pad1.33x1.80mm_HandSolder -> Capacitor_SMD:C_0805_2012Metric_Pad1.18x1.45mm_HandSolder; moved to F.Cu
- C7: value 0.1u -> 100n; footprint Capacitor_SMD:C_1206_3216Metric_Pad1.33x1.80mm_HandSolder -> Capacitor_SMD:C_0805_2012Metric_Pad1.18x1.45mm_HandSolder
- D1: value TD301MCANFD -> ~; footprint Package_TO_SOT_SMD:SOT-23-3 -> Diode_SMD:D_SOD-323_HandSoldering
- D11: value D_TVS_Small -> ~; footprint Diode_SMD:D_SMB_Handsoldering -> LED_SMD:LED_0805_2012Metric
- D12: value D_Schottky_Small -> D_TVS_Small; footprint Diode_SMD:D_SMA_Handsoldering -> Diode_SMD:D_SMB_Handsoldering
- D14, D8: value ~ -> D_Schottky_Small; footprint LED_SMD:LED_0805_2012Metric -> Diode_SMD:D_SMA_Handsoldering
- D16: value DS90LV019 -> ~; footprint Package_SO:SO-14_3.9x8.65mm_P1.27mm -> LED_SMD:LED_0805_2012Metric
- D17, D18, D19, D20, D21, D22, D23: value DS90LV019 -> ~; footprint Package_SO:SO-14_3.9x8.65mm_P1.27mm -> Package_SO:SO-8_3.9x4.9mm_P1.27mm
- D2: value ~ -> TD301MCANFD; footprint Package_TO_SOT_SMD:SOT-23 -> MORNSUN:TD5(3)01MCANFD; moved to F.Cu
- D3: footprint Package_TO_SOT_SMD:SOT-23-3 -> Package_TO_SOT_SMD:SOT-23
- D4: footprint LED_SMD:LED_0603_1608Metric_Pad1.05x0.95mm_HandSolder -> LED_SMD:LED_0805_2012Metric
- D5: value K7809T -> ~; footprint MORNSUN:K78xxT-1000R3 -> LED_SMD:LED_0805_2012Metric; moved to F.Cu
- D6: value URB2415LD-20WR3 -> K7809T; footprint MORNSUN:URB_LD-20WR3 -> MORNSUN:K78xxT-1000R3
- D7: value D_Schottky_Small -> URB2415LD-20WR3; footprint Diode_SMD:D_SMA_Handsoldering -> MORNSUN:URB_LD-20WR3
- J1: value Power_IN -> ~; footprint Connector_Molex:Molex_Mini-Fit_Jr_5566-04A_2x02_P4.20mm_Vertical -> Connector_PinHeader_2.54mm:PinHeader_1x04_P2.54mm_Vertical
- J2: value PSFB_Control_1 -> Power_IN; footprint Connector_IDC:IDC-Header_2x10_P2.54mm_Vertical -> Connector_Molex:Molex_Mini-Fit_Jr_5566-04A_2x02_P4.20mm_Vertical
- J3, J4: value PSFB_Control_1 -> ~; footprint Connector_IDC:IDC-Header_2x10_P2.54mm_Vertical -> Connector_FFC-FPC:Hirose_FH12-20S-0.5SH_1x20-1MP_P0.50mm_Horizontal
- L1: moved to F.Cu
- R1, R2: value 1k -> 10k; footprint Resistor_SMD:R_0603_1608Metric_Pad0.98x0.95mm_HandSolder -> Resistor_SMD:R_0805_2012Metric_Pad1.20x1.40mm_HandSolder
- R10: value 3k -> 10
- R12: value 249k -> 0
- R13: value 59k -> 3k
- R14: value 10k -> 1k
- R15: value 240k -> 249k
- R16: value 93.1k -> 59k
- R17: value 51k -> 10k
- R18: value 143k -> 240k
- R19: value 10k -> 93.1k
- R20: value 10k -> 51k
- R21: value 100 -> 143k
- R22: value 0 -> 10k
- R23: value 10m -> 10k; footprint Resistor_SMD:R_2512_6332Metric_Pad1.40x3.35mm_HandSolder -> Resistor_SMD:R_0805_2012Metric_Pad1.20x1.40mm_HandSolder
- R25: value 3k -> 0
- R26: value 3k -> 10m; footprint Resistor_SMD:R_0805_2012Metric_Pad1.20x1.40mm_HandSolder -> Resistor_SMD:R_2512_6332Metric_Pad1.40x3.35mm_HandSolder
- R27: value 0 -> 100
- R28: value 0 -> 470
- R29: value 470 -> 3k
- R3, R4: value 59 -> 20
- R30: value 0 -> 3k
- R34, R39, R44: value 470 -> 0
- R5: value 1k -> 59; footprint Resistor_SMD:R_0603_1608Metric_Pad0.98x0.95mm_HandSolder -> Resistor_SMD:R_0805_2012Metric_Pad1.20x1.40mm_HandSolder
- R6: value 2k -> 59
- R7: value 10 -> 1k
- R9: value 0 -> 2k
- U2: footprint Package_QFP:LQFP-64_10x10mm_P0.5mm -> Package_TO_SOT_SMD:SOT-23-6
- U3: value AMS1117-5.0 -> ~; footprint Package_TO_SOT_SMD:SOT-223-3_TabPin2 -> Package_QFP:LQFP-64_10x10mm_P0.5mm
- U4: value AMS1117-3.3 -> AMS1117-5.0
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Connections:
- C11 pad 1: +3.3V -> Net-(C11-Pad1)
- C11 pad 2: GND -> GND_CAN
- C12 pad 1: +3.3V -> Net-(U3-VCAP_1)
- C13 pad 1: Net-(U2-VCAP_1) -> Net-(U3-VCAP_2)
- C14 pad 1: Net-(U2-VCAP_2) -> +3.3V
- C15 pad 1: Net-(U5-VIN) -> +3.3V
- C15 pad 2: GND_IN -> GND
- C16 pad 1: VCC -> +3.3V
- C16 pad 2: GND_IN -> GND
- C17 pad 1: +24V -> +3.3V
- C17 pad 2: GND_IN -> GND
- C18 pad 1: GND_IN -> Net-(U6-VIN)
- C18 pad 2: VIN_filtered -> GND_IN
- C19 pad 1: VIN_filtered -> VCC
- C2 pad 1: +3.3V -> GND
- C2 pad 2: GND -> NRST
- C20 pad 1: GND_IN -> +24V
- C20 pad 2: VIN_filtered -> GND_IN
- C21 pad 2: +24V -> VIN_filtered
- C22 pad 1: GND_IN -> VIN_filtered
- C22 pad 2: +24V -> GND_IN
- C23 pad 1: +24V -> GND_IN
- C23 pad 2: GND_IN -> VIN_filtered
- C25 pad 1: GND -> GND_IN
- C25 pad 2: +15V -> +24V
- C26 pad 1: GND -> +24V
- C26 pad 2: +9V -> GND_IN
- C27 pad 1: GND -> GND_IN
- C27 pad 2: +5V -> +24V
- C28 pad 2: +5V -> +15V
- C29 pad 2: +3.3V -> +9V
- C3 pad 1: +3.3V -> GND
- C3 pad 2: GND -> Net-(U3-PH0)
- C30 pad 1: Net-(U5-COMP) -> GND
- C30 pad 2: Net-(C30-Pad2) -> +5V
- C31 pad 1: Net-(U5-SS) -> GND
- C31 pad 2: GND_IN -> +5V
- C32 pad 1: Net-(U5-COMP) -> GND
- C32 pad 2: GND_IN -> +3.3V
- C33 pad 1: /SW1 -> Net-(U6-COMP)
- C33 pad 2: Net-(D12-K) -> Net-(C33-Pad2)
- C34 pad 1: Net-(U5-SLOPE) -> Net-(U6-SS)
- C35 pad 1: /SW2 -> Net-(U6-COMP)
- C35 pad 2: Net-(D13-K) -> GND_IN
- C36 pad 1: Net-(U5-CSG) -> /SW1
- C36 pad 2: Net-(U5-CS) -> Net-(D13-K)
- C37 pad 1: +3.3V -> Net-(U6-SLOPE)
- C37 pad 2: GND -> GND_IN
- C38 pad 1: +3.3V -> /SW2
- C38 pad 2: GND -> Net-(D14-K)
- C39 pad 1: +3.3V -> Net-(U6-CSG)
- C39 pad 2: GND -> Net-(U6-CS)
- C4 pad 1: +3.3V -> Net-(U3-PH1)
- C40 pad 1: +3.3V -> /ERROR_Channel_1
- C41 pad 1: /FAULT1 -> +3.3V
- C46 pad 1: /FAULT2 -> +3.3V
- C51 pad 1: /FAULT3 -> +3.3V
- C56 pad 1: /FAULT4 -> +3.3V
- C8 pad 1: Net-(C8-Pad1) -> +3.3V
- C8 pad 2: GND_CAN -> GND
- D1 pad 1: CAN1_RXD_MCU -> +3.3V
- D1 pad 2: CAN1_TXD_MCU -> Net-(D1-A)
- D10 pad 2: +3.3V -> +15V
- D11 pad 1: GND_IN -> Net-(D11-K)
- D11 pad 2: VIN_filtered -> +3.3V
- D12 pad 1: Net-(D12-K) -> GND_IN
- D12 pad 2: VCC -> VIN_filtered
- D14 pad 2: VIN -> VCC
- D15 pad 2: +24V -> VIN
- D16 pad 1: +3.3V -> Net-(D16-K)
- D16 pad 2: /TMR1_CH1N -> +24V
- D17 pad 1: +3.3V -> unconnected-(D17-RO-Pad1)
- D17 pad 2: /TMR1_CH1 -> GND
- D17 pad 3: (no net) -> +3.3V
- D17 pad 4: unconnected-(D17-ROUT-Pad4) -> /TMR1_CH1N
- D17 pad 5: (no net) -> GND
- D17 pad 6: (no net) -> Net-(D17-A)
- D17 pad 7: GND -> Net-(D17-B)
- D17 pad 8: GND -> +3.3V
- D18 pad 1: +3.3V -> unconnected-(D18-RO-Pad1)
- D18 pad 2: /TMR1_CH2N -> GND
- D18 pad 3: (no net) -> +3.3V
- D18 pad 4: unconnected-(D18-ROUT-Pad4) -> /TMR1_CH1
- D18 pad 5: (no net) -> GND
- D18 pad 6: (no net) -> Net-(D18-A)
- D18 pad 7: GND -> Net-(D18-B)
- D18 pad 8: GND -> +3.3V
- D19 pad 1: +3.3V -> unconnected-(D19-RO-Pad1)
- D19 pad 2: /TMR1_CH2 -> GND
- D19 pad 3: (no net) -> +3.3V
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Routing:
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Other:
- board text removed: "CPU VER1.0"
- board text removed: "PWR"
- board text removed: "USER"
